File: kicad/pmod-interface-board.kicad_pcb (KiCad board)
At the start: 4 copper layers, 81.7 x 61 mm, 30 parts, among them J1 PMOD Connector 1, J2 PMOD Connector 2, J4 Gameboy Cart Connector, U1 74HCT541, U2 74HCT541, U3 74HC595, U4 74HC595, U5 74HC595, U6 74HC597

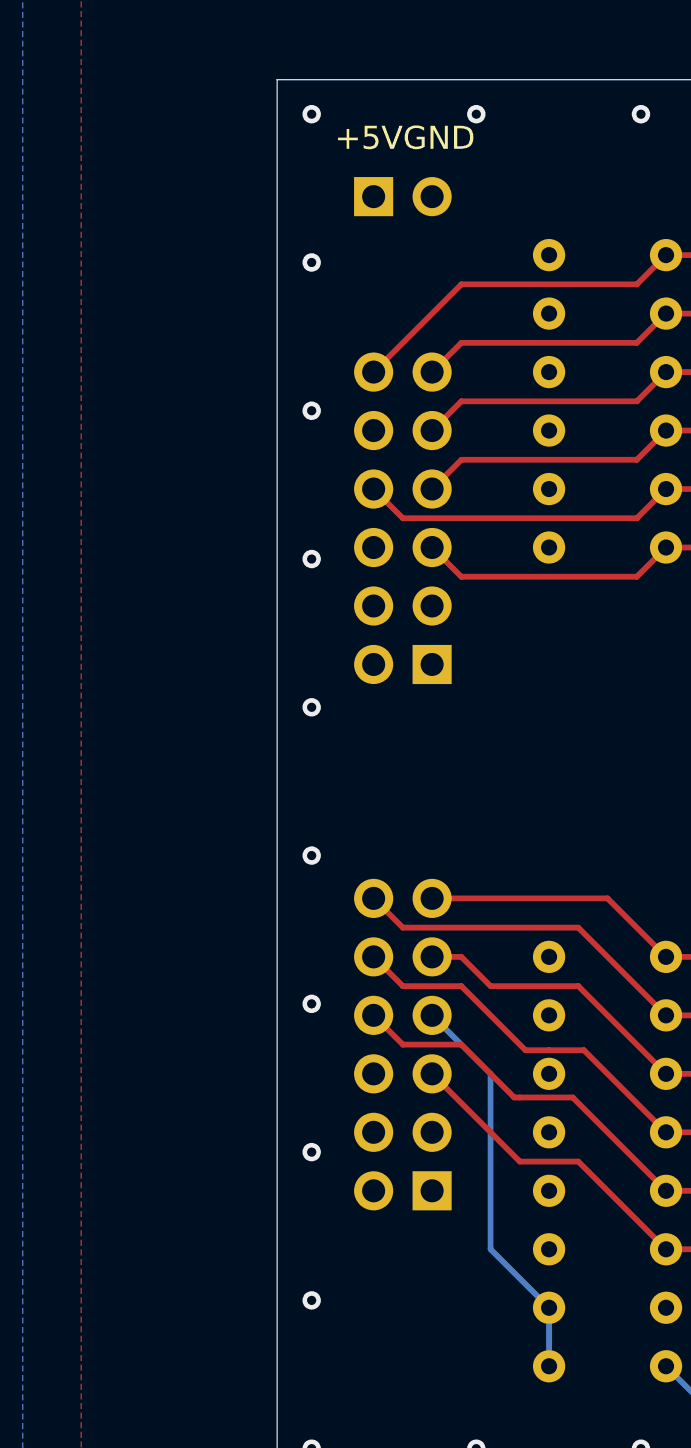
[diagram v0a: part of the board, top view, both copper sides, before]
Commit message: kicad: narrowed thermal relief spokes and added copper pour to +5v header
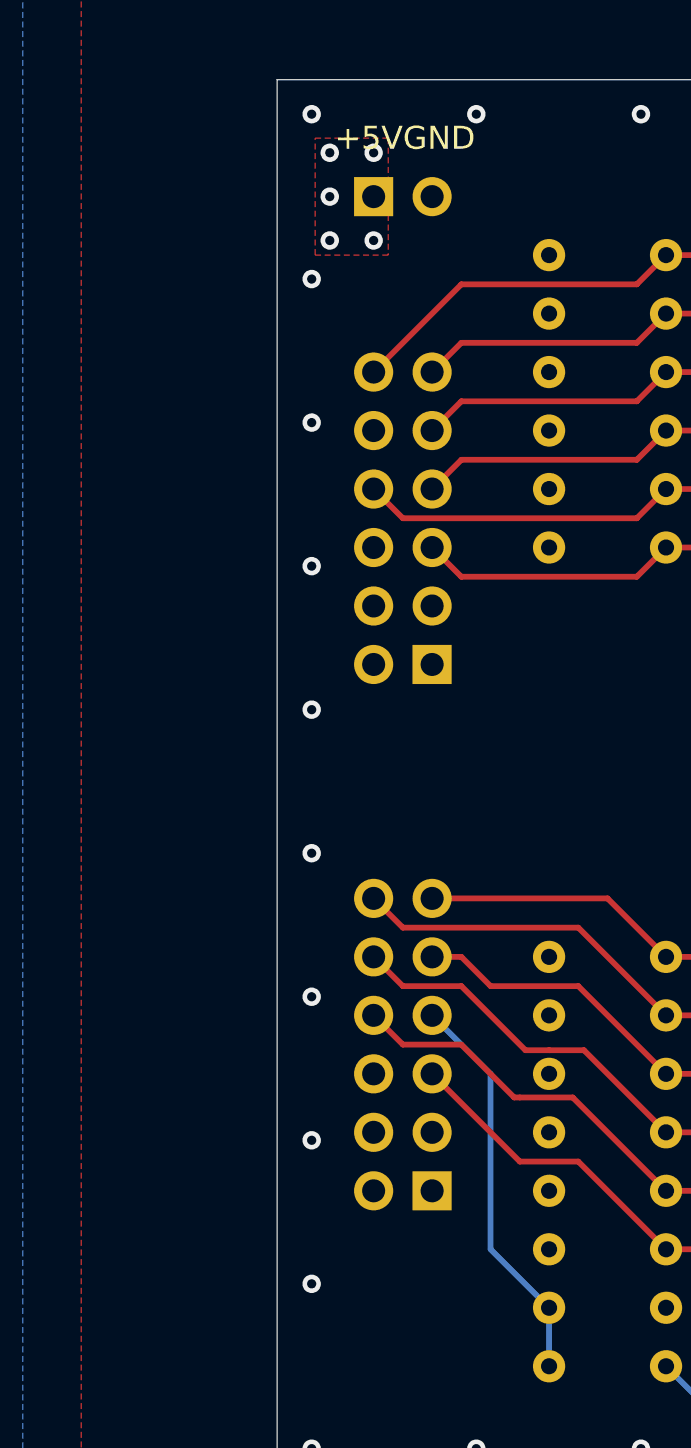
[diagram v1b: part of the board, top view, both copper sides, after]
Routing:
- net +5V: vias 4 -> 9
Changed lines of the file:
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@@
+	)
+	(via
+		(at 112.395 66.04)
+		(size 0.8)
+		(drill 0.4)
+		(layers "F.Cu" "B.Cu")
+		(free yes)
+		(net 1)
+	)
+	(via
+		(at 112.395 64.135)
+		(size 0.8)
+		(drill 0.4)
+		(layers "F.Cu" "B.Cu")
+		(free yes)
+		(net 1)
+	)
+	(via
+		(at 112.395 67.945)
+		(size 0.8)
+		(drill 0.4)
+		(layers "F.Cu" "B.Cu")
+		(free yes)
+		(net 1)
+	)
+	(via
+		(at 114.3 64.135)
+		(size 0.8)
+		(drill 0.4)
+		(layers "F.Cu" "B.Cu")
+		(free yes)
+		(net 1)
 	)
 	(via
@@
 	)
 	(via
+		(at 114.3 67.945)
+		(size 0.8)
+		(drill 0.4)
+		(layers "F.Cu" "B.Cu")
+		(free yes)
+		(net 1)
+	)
+	(via
 		(at 190.27 113.98)
 		(size 0.8)
@@
 	)
 	(via
-		(at 111.609 75.34)
+		(at 111.609 75.854286)
 		(size 0.8)
 		(drill 0.4)
@@
 	)
 	(via
-		(at 111.609 101.1)
-		(size 0.8)
-		(drill 0.4)
-		(layers "F.Cu" "B.Cu")
-		(free yes)
-		(net 2)
-	)
-	(via
-		(at 111.609 113.98)
+		(at 111.609 100.791429)
+		(size 0.8)
+		(drill 0.4)
+		(layers "F.Cu" "B.Cu")
+		(free yes)
+		(net 2)
+	)
+	(via
+		(at 111.609 113.26)
 		(size 0.8)
 		(drill 0.4)
@@
 	)
 	(via
-		(at 111.609 81.78)
+		(at 111.609 82.088571)
 		(size 0.8)
 		(drill 0.4)
@@
 	)
 	(via
-		(at 111.609 107.54)
-		(size 0.8)
-		(drill 0.4)
-		(layers "F.Cu" "B.Cu")
-		(free yes)
-		(net 2)
-	)
-	(via
-		(at 111.609 94.66)
+		(at 111.609 107.025714)
+		(size 0.8)
+		(drill 0.4)
+		(layers "F.Cu" "B.Cu")
+		(free yes)
+		(net 2)
+	)
+	(via
+		(at 111.609 94.557143)
 		(size 0.8)
 		(drill 0.4)
@@
 	(via
 		(at 133.062 120.42)
-		(size 0.8)
-		(drill 0.4)
-		(layers "F.Cu" "B.Cu")
-		(free yes)
-		(net 2)
-	)
-	(via
-		(at 111.609 68.9)
 		(size 0.8)
 		(drill 0.4)
@@
 	)
 	(via
+		(at 111.61 69.62)
+		(size 0.8)
+		(drill 0.4)
+		(layers "F.Cu" "B.Cu")
+		(free yes)
+		(net 2)
+	)
+	(via
 		(at 190.27 101.1)
 		(size 0.8)
@@
 	)
 	(via
-		(at 111.609 88.22)
+		(at 111.609 88.322857)
 		(size 0.8)
 		(drill 0.4)
@@
 		(filled_areas_thickness no)
 		(fill yes
-			(thermal_gap 0.5)
-			(thermal_bridge_width 0.5)
+			(thermal_gap 0.25)
+			(thermal_bridge_width 0.4)
 		)
 		(polygon
@@
 	)
 	(zone
+		(net 1)
+		(net_name "+5V")
+		(layer "F.Cu")
+		(hatch edge 0.5)
+		(priority 5)
+		(connect_pads yes
+			(clearance 0.25)
+		)
+		(min_thickness 0.25)
+		(filled_areas_thickness no)
+		(fill yes
+			(thermal_gap 0.5)
+			(thermal_bridge_width 0.5)
+			(smoothing fillet)
+			(radius 0.5)
+		)
+		(polygon
+			(pts
+				(xy 114.935 68.58) (xy 111.76 68.58) (xy 111.76 63.5) (xy 114.935 63.5)
+			)
+		)
+	)
+	(zone
 		(net 2)
 		(net_name "GND")
@@
 		(filled_areas_thickness no)
 		(fill yes
-			(thermal_gap 0.5)
-			(thermal_bridge_width 0.5)
+			(thermal_gap 0.25)
+			(thermal_bridge_width 0.4)
 		)
 		(polygon
@@
 		(filled_areas_thickness no)
 		(fill yes
-			(thermal_gap 0.5)
-			(thermal_bridge_width 0.5)
+			(thermal_gap 0.25)
+			(thermal_bridge_width 0.4)
 		)
 		(polygon
@@
 		(filled_areas_thickness no)
 		(fill yes
-			(thermal_gap 0.5)
-			(thermal_bridge_width 0.5)
+			(thermal_gap 0.25)
+			(thermal_bridge_width 0.4)
 		)
 		(polygon

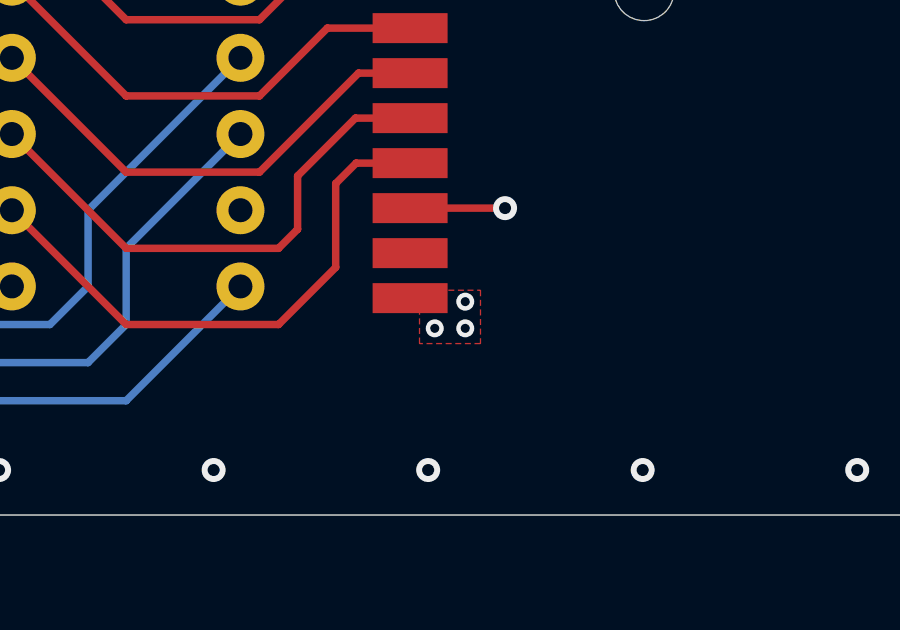
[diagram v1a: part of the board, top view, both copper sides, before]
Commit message: kicad: added keepout zone to make the cart connections more appealing
There were less than a handful of GND fill between some of these traces so we might aswell just remove them so it looks better. Should have little to no impact on performance.
Also adjusted the GND via pour to make it symmetric to the +5V one.
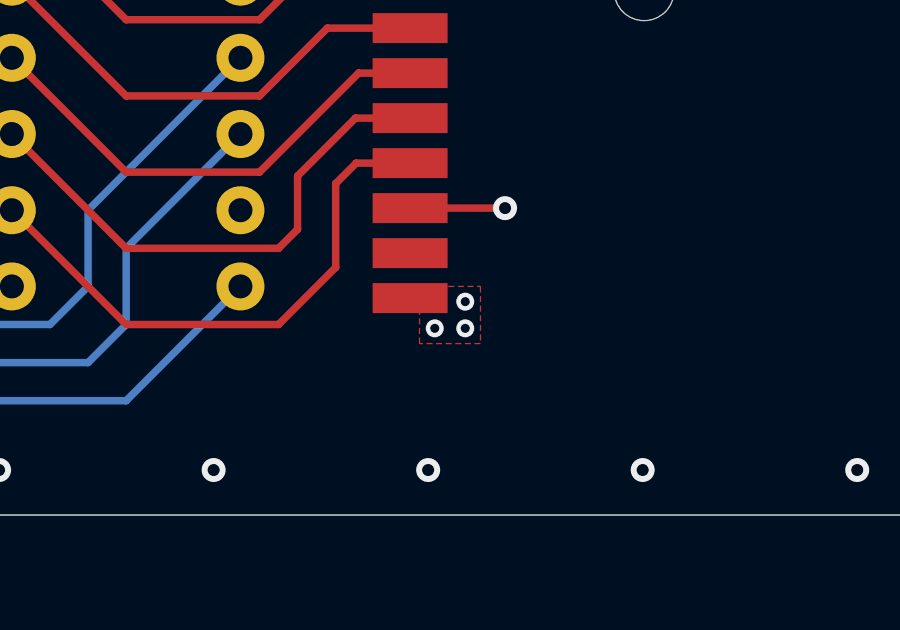
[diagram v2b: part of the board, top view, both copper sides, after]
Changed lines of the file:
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@@
+	)
+	(zone
+		(net 0)
+		(net_name "")
+		(layer "F.Cu")
+		(hatch edge 0.5)
+		(connect_pads
+			(clearance 0)
+		)
+		(min_thickness 0.25)
+		(filled_areas_thickness no)
+		(keepout
+			(tracks allowed)
+			(vias allowed)
+			(pads allowed)
+			(copperpour not_allowed)
+			(footprints allowed)
+		)
+		(placement
+			(enabled no)
+			(sheetname "/")
+		)
+		(fill
+			(thermal_gap 0.5)
+			(thermal_bridge_width 0.5)
+		)
+		(polygon
+			(pts
+				(xy 162.56 82.55) (xy 163.83 81.28) (xy 162.56 80.01) (xy 162.56 69.85) (xy 166.37 73.66) (xy 166.37 109.22)
+				(xy 162.56 109.22) (xy 162.56 96.52) (xy 163.83 96.52) (xy 163.83 93.98) (xy 162.56 92.71)
+			)
+		)
 	)
 	(zone
@@
 		(polygon
 			(pts
-				(xy 168.529 114.427) (xy 170.561 114.427) (xy 170.561 116.205) (xy 168.529 116.205)
+				(xy 168.529 114.3) (xy 170.561 114.3) (xy 170.561 116.205) (xy 168.529 116.205)
 			)
 		)

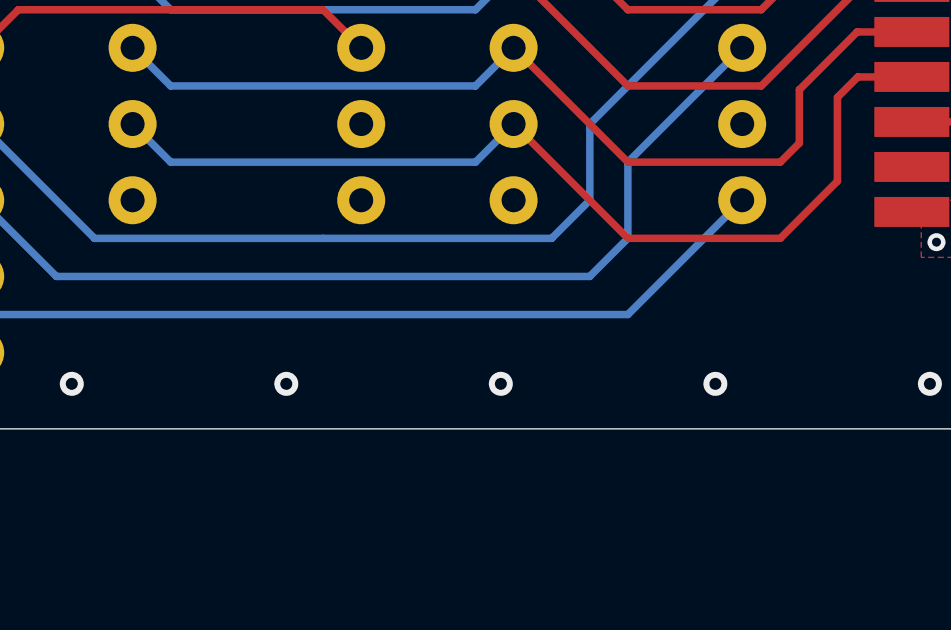
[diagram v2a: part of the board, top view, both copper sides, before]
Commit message: kicad: added revision and date silkscreen - board is complete
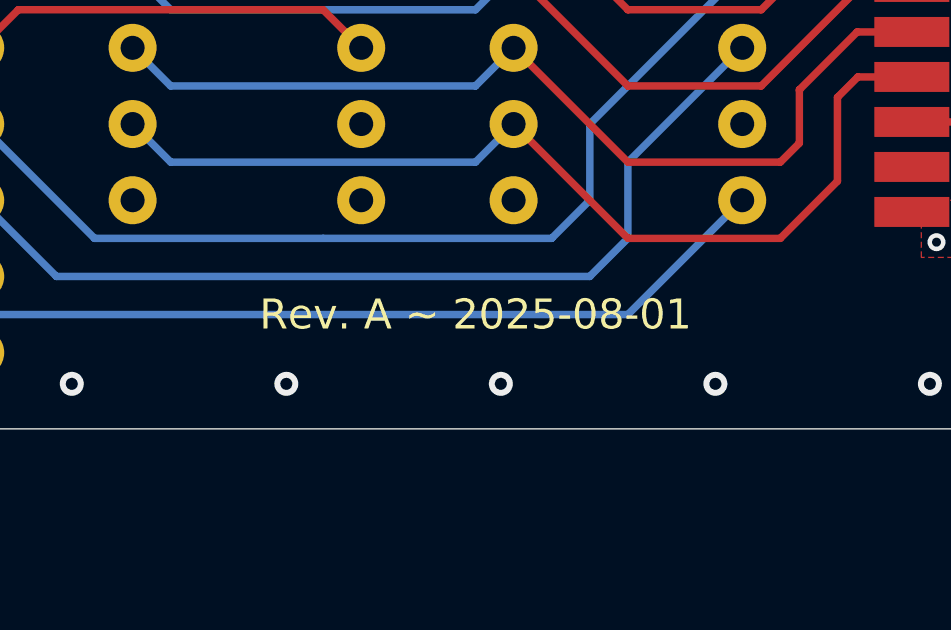
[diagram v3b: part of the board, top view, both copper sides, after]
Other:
- board text added: "Rev. A ~ 2025-08-01"
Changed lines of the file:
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@@
 	(title_block
 		(title "GB Cart PMOD Interface Board")
+		(date "2025-08-01")
+		(rev "A")
 	)
 	(layers
@@
 		(layer "Edge.Cuts")
 	)
+	(gr_text "Rev. A ~ 2025-08-01"
+		(at 153.67 118.11 0)
+		(layer "F.SilkS")
+		(effects
+			(font
+				(size 1 1)
+				(thickness 0.15)
+			)
+		)
+	)
 	(gr_text "+5V"

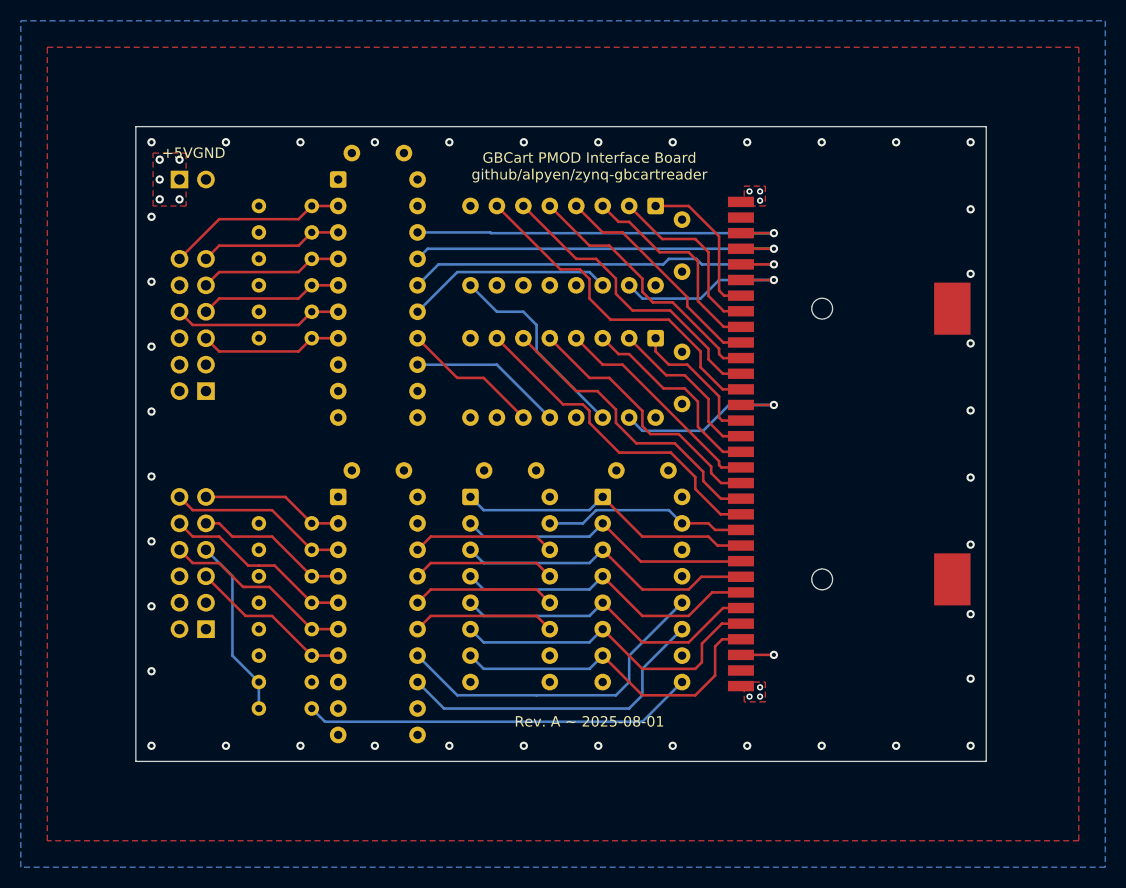
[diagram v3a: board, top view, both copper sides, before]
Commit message: kicad: fixed faulty 597 wiring and moved pullups to +3.3v
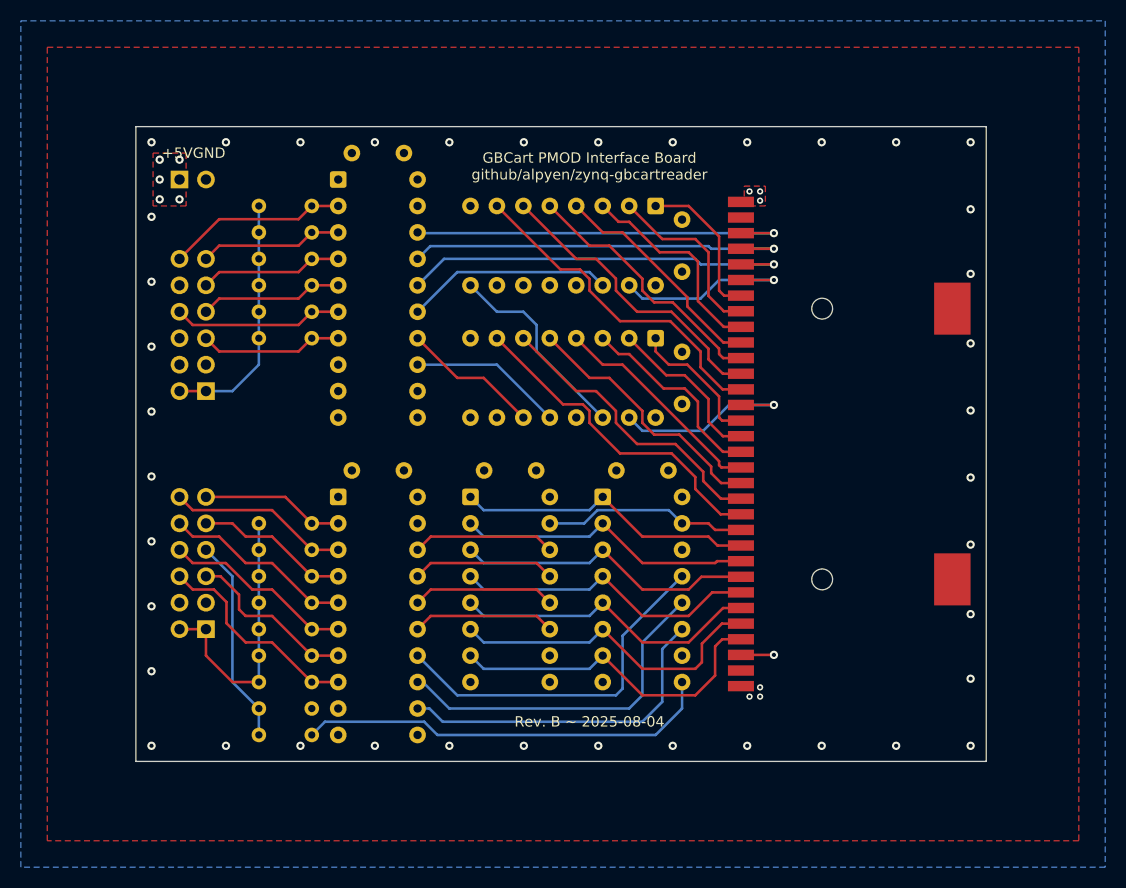
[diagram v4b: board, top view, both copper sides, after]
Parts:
- added R13: 10K, Resistor_THT:R_Axial_DIN0204_L3.6mm_D1.6mm_P5.08mm_Horizontal, F.Cu at (121.9, 114.3)
- moved R15 2.54 mm to (121.9, 116.8)
- moved R14 2.54 mm to (127.0, 119.4)
- renumbered R13 to R14, R14 to R15
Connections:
- J1 pad 1: unconnected-(J1-Pin_1-Pad1) -> +3.3V
- J1 pad 2: unconnected-(J1-Pin_2-Pad2) -> +3.3V
- J2 pad 1: unconnected-(J2-Pin_1-Pad1) -> +3.3V
- J2 pad 2: unconnected-(J2-Pin_2-Pad2) -> +3.3V
- J2 pad 5: DATA_IN_SCLK_in -> DATA_IN_RCLK_in
- J2 pad 6: unconnected-(J2-Pin_6-Pad6) -> DATA_IN_SCLK_in
- J2 pad 8: DATA_IN_RCLK_in -> DATA_IN_PL_in
- R1 pad 1: +5V -> +3.3V
- R10 pad 1: +5V -> +3.3V
- R11 pad 1: +5V -> +3.3V
- R11 pad 2: DATA_IN_RCLK_in -> DATA_IN_PL_in
- R12 pad 1: +5V -> +3.3V
- R12 pad 2: DATA_IN_SCLK_in -> DATA_IN_RCLK_in
- R2 pad 1: +5V -> +3.3V
- R3 pad 1: +5V -> +3.3V
- R4 pad 1: +5V -> +3.3V
- R5 pad 1: +5V -> +3.3V
- R6 pad 1: +5V -> +3.3V
- R7 pad 1: +5V -> +3.3V
- R8 pad 1: +5V -> +3.3V
- R9 pad 1: +5V -> +3.3V
- U2 pad 12: unconnected-(U2-Y6-Pad12) -> /DATA_IN_SCLK
- U2 pad 13: /DATA_IN_SCLK -> /DATA_IN_RCLK
- U2 pad 14: /DATA_IN_RCLK -> /DATA_IN_PL
- U2 pad 6: DATA_IN_RCLK_in -> DATA_IN_PL_in
- U2 pad 7: DATA_IN_SCLK_in -> DATA_IN_RCLK_in
- U2 pad 8: GND -> DATA_IN_SCLK_in
- U6 pad 13: GND -> /DATA_IN_PL
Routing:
- net +3.3V: track 0.00 -> 50.4 mm
- net /DATA_IN_PL: track 0.00 -> 34.7 mm
- net DATA_IN_PL_in: track 0.00 -> 18.4 mm
- net DATA_IN_SCLK_in: track 15.9 -> 20.6 mm
- net Net-(U6-Q7): track 37.7 -> 40.2 mm
- net DATA_IN_SDATA_out: track 17.3 -> 19.9 mm
- net DATA_IN_RCLK_in: track 18.4 -> 16.7 mm
- net /DATA_IN_SCLK: track 31.1 -> 32.6 mm
- net /DATA_IN_RCLK: track 32.1 -> 33.1 mm
- net /A4: track 22.4 -> 21.8 mm
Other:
- board text added: "10K"
- board text added: "Rev. B ~ 2025-08-04"
- board text removed: "Rev. A ~ 2025-08-01"
